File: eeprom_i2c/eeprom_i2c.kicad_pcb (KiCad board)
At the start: 2 copper layers, 25 x 36 mm, 7 parts, among them J1 Conn_01x03_Pin, J2 Conn_01x03_Pin, J3 Conn_01x03_Pin, J4 1x4 strip 2.54mm, U1 24LC256

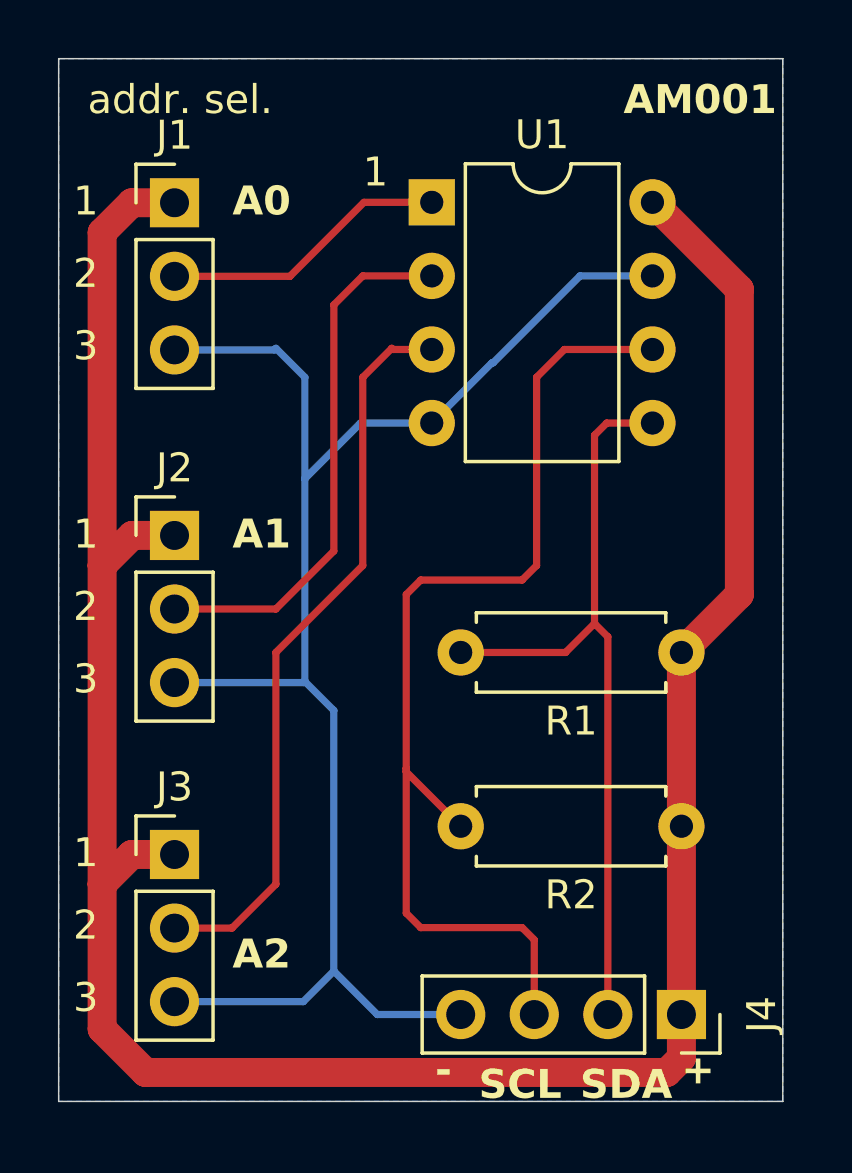
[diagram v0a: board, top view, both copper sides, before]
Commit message: Add by-pass capacitor; add mounting hole and change main connector's pinout.
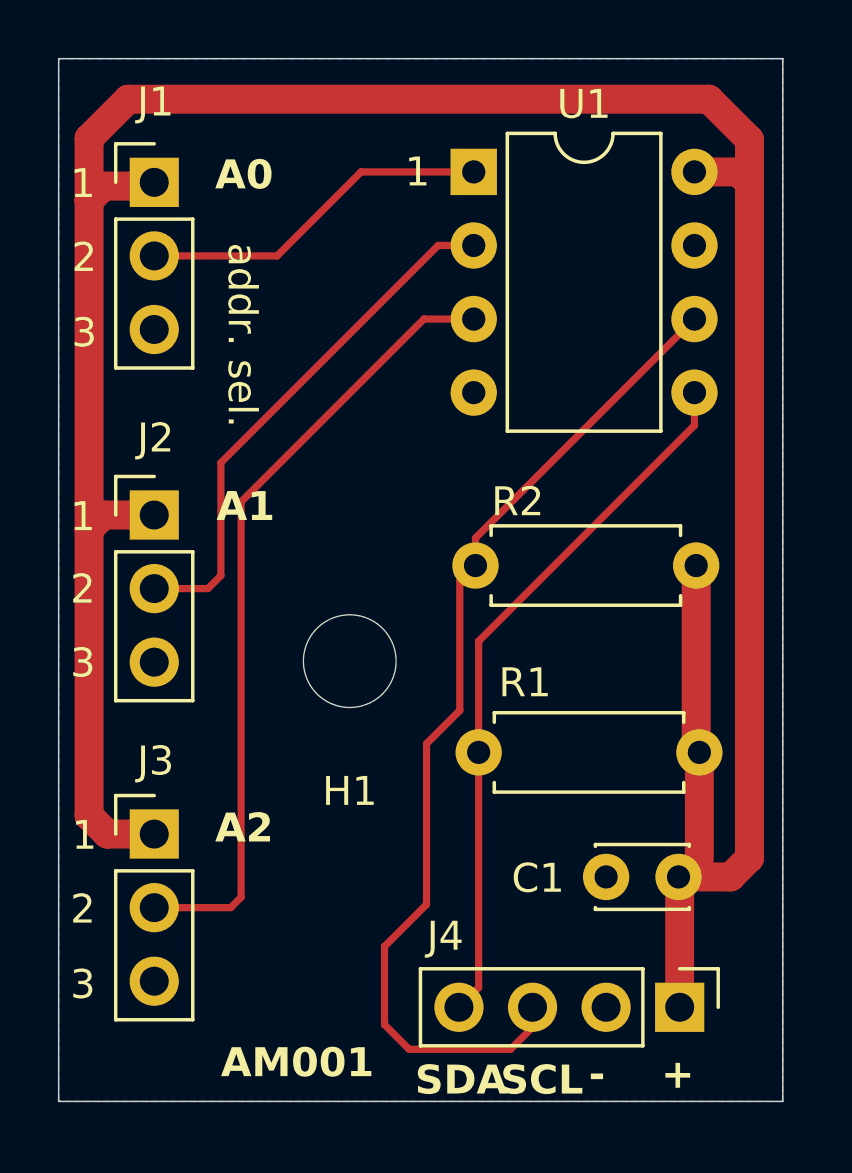
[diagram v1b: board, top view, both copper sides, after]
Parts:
- added C1: 100nf, Capacitor_THT:C_Disc_D3.0mm_W2.0mm_P2.50mm, F.Cu at (143.4, 88.2)
- added H1: MountingHole, MountingHole:MountingHole_3.2mm_M3, F.Cu at (132.1, 80.8)
- J4: footprint Connector_PinSocket_2.54mm:PinSocket_1x04_P2.54mm_Vertical -> Connector_PinHeader_2.54mm:PinHeader_1x04_P2.54mm_Vertical
- moved R2 9.01 mm to (144.0, 77.5)
- moved R1 3.51 mm to (144.1, 84.0)
- moved U1 1.79 mm to (136.3, 63.9)
- moved J1 0.99 mm to (125.3, 64.3)
- moved J2 0.99 mm to (125.3, 75.8)
- moved J3 0.99 mm to (125.3, 86.8)
- moved J4 0.26 mm to (143.4, 92.8)
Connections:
- net VCC renamed Net-(J1-Pin_1)
- J4 pad 2: Net-(J4-SDA) -> GND
- J4 pad 4: GND -> Net-(J4-SDA)
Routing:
- net GND: track 56.2 -> 0.00 mm
- net Net-(J1-Pin_1): track 88.7 -> 99.9 mm
- net Net-(J4-SDA): track 27.4 -> 24.6 mm
- net Net-(J1-Pin_2): track 9.94 -> 12.2 mm
- net Net-(J3-Pin_2): track 25.7 -> 27.4 mm
- net Net-(J4-SCL): track 37.0 -> 35.3 mm

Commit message: Change the position of C1 (close to Vcc PIN of U1). Add gerber for F_Mask e B_Mask.
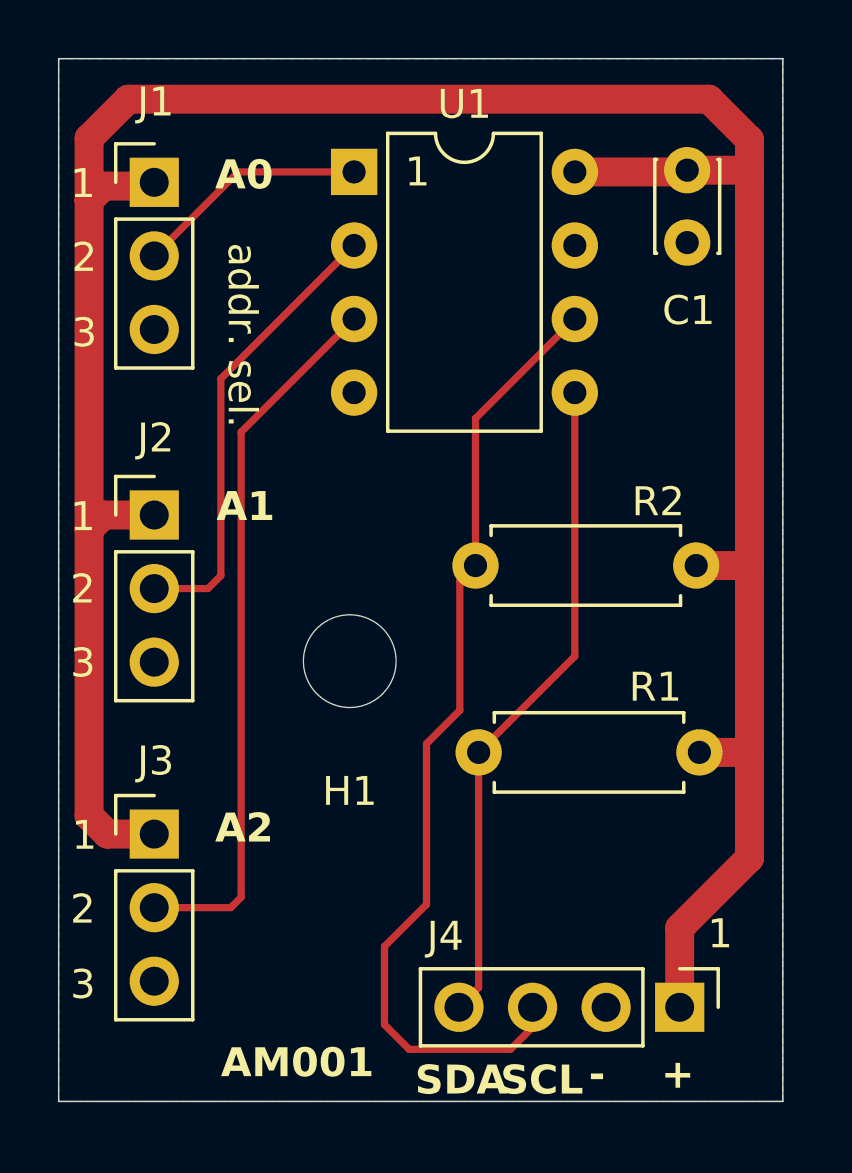
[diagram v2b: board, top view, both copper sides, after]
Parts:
- moved C1 24.4 mm to (143.7, 63.9), turned to -90 degrees
- moved U1 4.13 mm to (132.2, 63.9)
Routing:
- net Net-(J1-Pin_1): track 99.9 -> 95.6 mm
- net Net-(J1-Pin_2): track 12.2 -> 8.10 mm
- net Net-(J3-Pin_2): track 27.4 -> 24.7 mm
- net Net-(J2-Pin_2): track 18.2 -> 15.8 mm
- net Net-(J4-SDA): track 24.6 -> 22.9 mm
- net Net-(J4-SCL): track 35.3 -> 33.5 mm

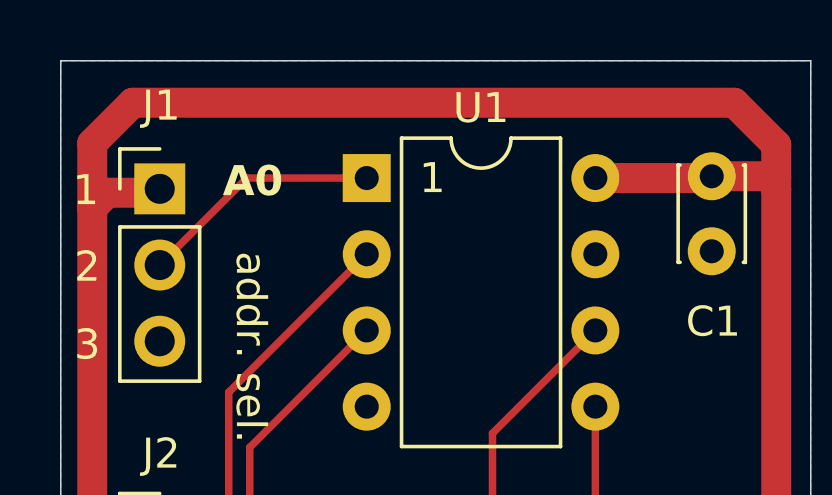
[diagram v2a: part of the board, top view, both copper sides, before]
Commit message: Update panel for production and fix label position (gerber regenerated).
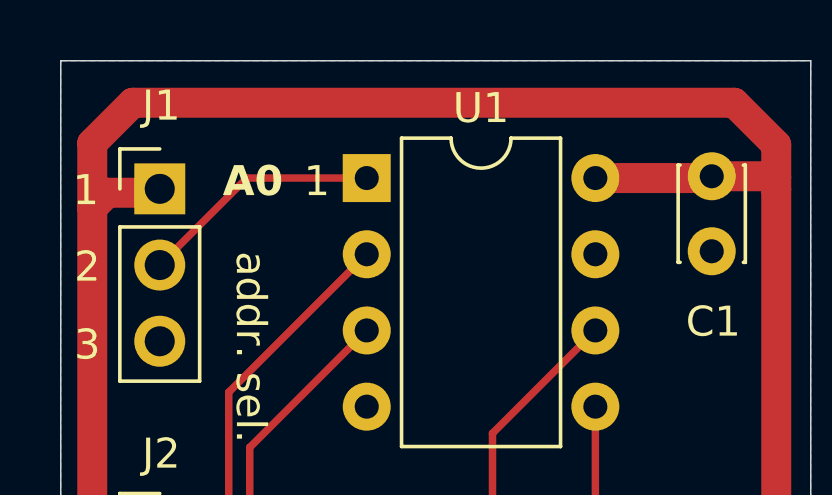
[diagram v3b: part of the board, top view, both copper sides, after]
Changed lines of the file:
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@@
 	)
 	(gr_text "1"
-		(at 133.95 64.5 0)
+		(at 130.1 64.6 0)
 		(layer "F.SilkS")
 		(effects
